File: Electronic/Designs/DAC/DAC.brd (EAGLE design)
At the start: 50 x 50 mm, 36 parts

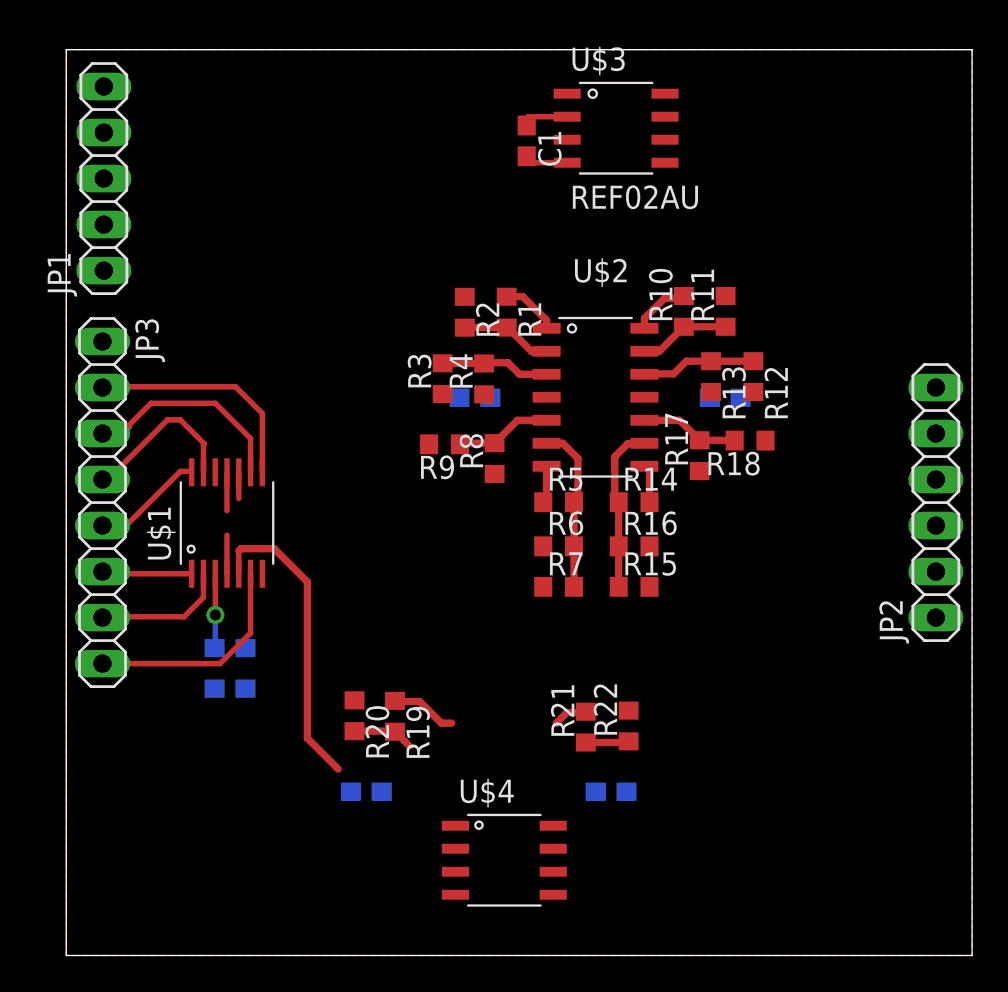
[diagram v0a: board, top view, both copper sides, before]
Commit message: adjusted adc pwr pins on board
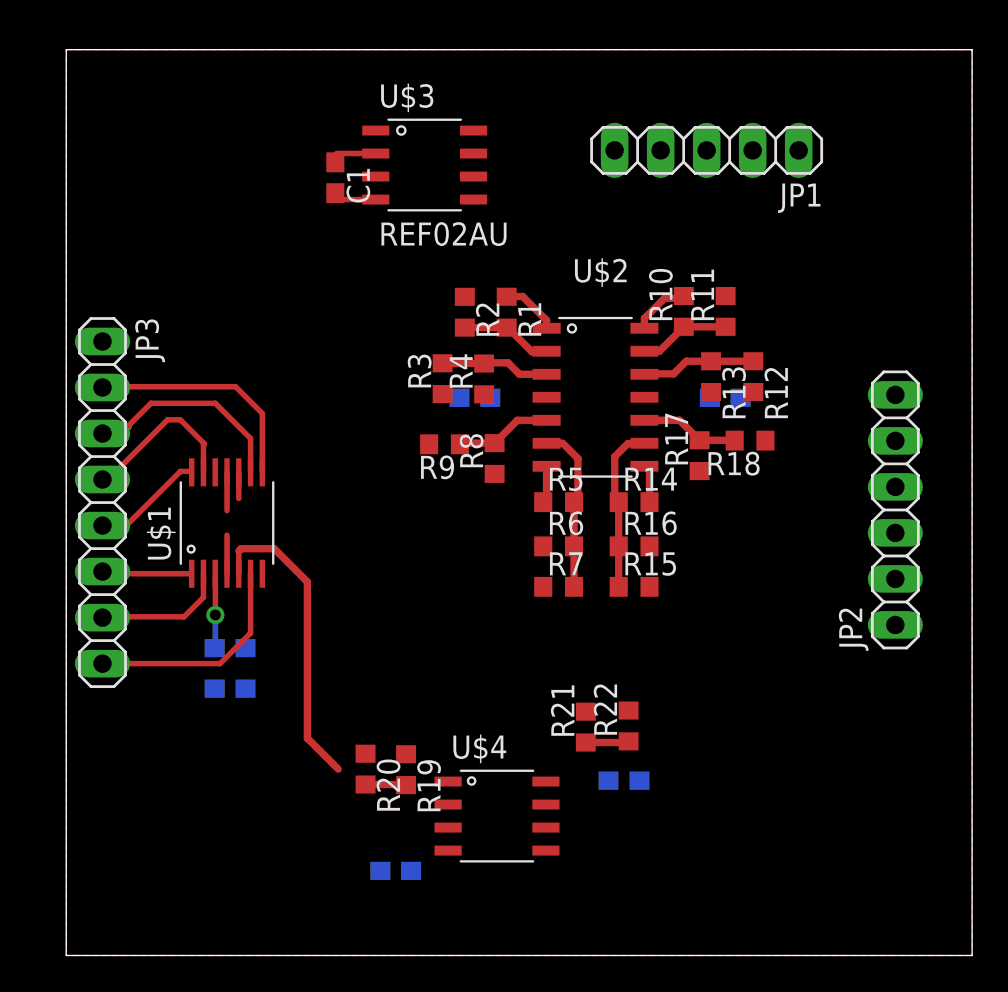
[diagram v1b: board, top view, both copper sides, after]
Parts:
- moved JP1 33.3 mm to (35.3, 44.4), turned to 180 degrees
- moved C7 14.2 mm to (30.8, 9.65), turned to 180 degrees
- moved C6 12.7 mm to (18.2, 4.67), turned to 0 degrees
- moved C1 10.8 mm to (14.9, 42.9)
- moved U$3 10.8 mm to (19.8, 43.0)
- moved R19 3.01 mm to (18.8, 10.3)
- moved R20 3.01 mm to (16.5, 10.3)
- moved U$4 2.47 mm to (23.8, 8.33)
- moved JP2 2.27 mm to (45.8, 24.6)
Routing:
- net N$21: track 3.64 -> 0.00 mm
- net BIAS: track 1.89 -> 0.00 mm
- net N$19: track 3.38 -> 2.25 mm

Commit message: split power pins from 5v and 15v
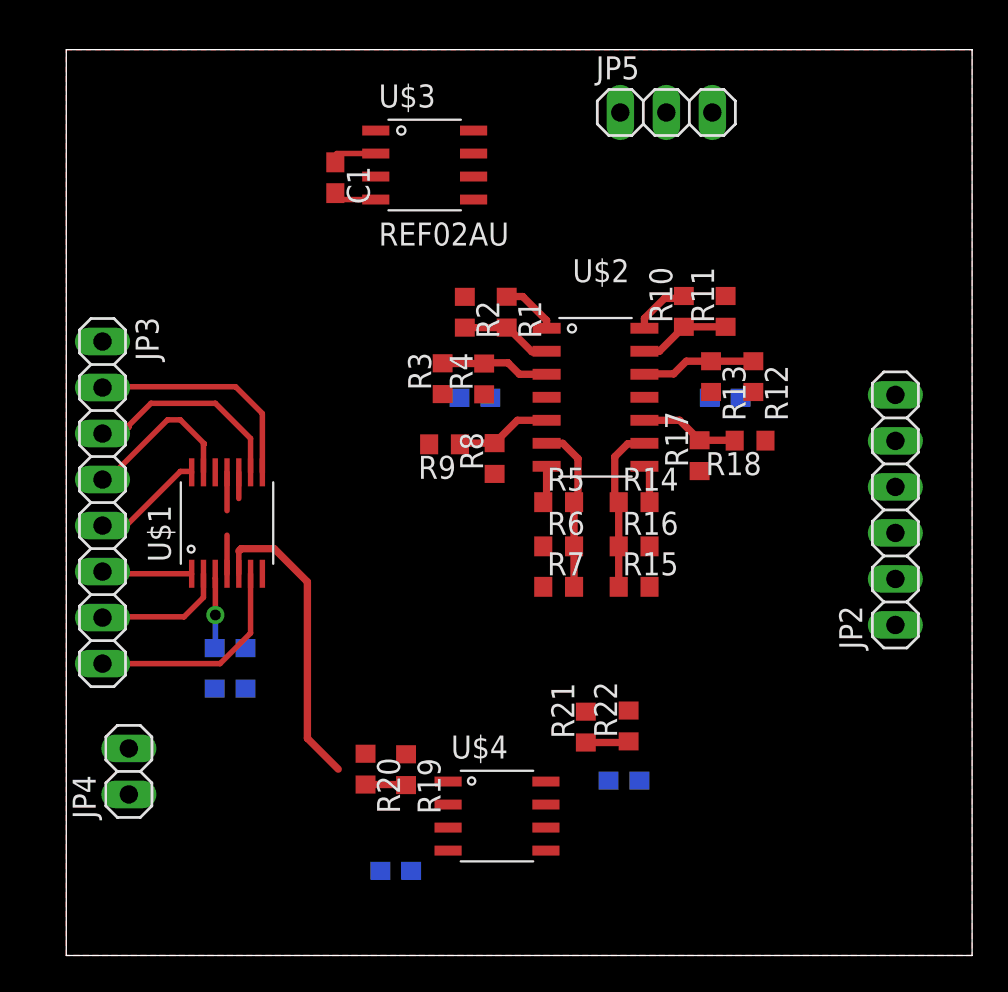
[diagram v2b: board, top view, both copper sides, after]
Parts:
- removed JP1: PWR, pinhead:1X05
- added JP4: (no value), pinhead:1X02
- added JP5: (no value), pinhead:1X03
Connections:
- net +15V: now also JP5.1; no longer JP1.4
- net +5V: now also JP4.2; no longer JP1.2
- net -15V: now also JP5.2; no longer JP1.5
- net GND: now also JP4.1, JP5.3; no longer JP1.1, JP1.3
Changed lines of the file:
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@@
 <elements>
 <element name="C1" library="resistor" package="C0603" value="0.1uf" x="14.8504" y="42.9308" rot="R270"/>
-<element name="JP1" library="pinhead" package="1X05" value="PWR" x="35.348" y="44.44" rot="R180"/>
 <element name="R1" library="resistor" package="R0603" value="40k" x="24.3116" y="35.5092" rot="R270"/>
 <element name="R10" library="resistor" package="R0603" value="40k" x="34.0896" y="35.5524" rot="R90"/>
@@
 <element name="C7" library="resistor" package="C0603" value="1uf" x="30.7848" y="9.652" rot="MR180"/>
 <element name="U$4" library="OPAX22X" package="SOIC-8" value="OPA2227UA" x="23.7744" y="8.3312"/>
+<element name="JP4" library="pinhead" package="1X02" value="" x="3.4544" y="10.16" rot="R90"/>
+<element name="JP5" library="pinhead" package="1X03" value="" x="33.1216" y="46.5328"/>
 </elements>
 <signals>
 <signal name="+5V">
 <contactref element="C3" pad="1"/>
-<contactref element="JP1" pad="2"/>
 <contactref element="U$1" pad="P$3"/>
 <contactref element="C2" pad="1"/>
@@
 <wire x1="8.2296" y1="18.796" x2="8.2296" y2="17.0044" width="0.3048" layer="16"/>
 <wire x1="8.2296" y1="17.0044" x2="8.1924" y2="16.9672" width="0.3048" layer="16"/>
-<wire x1="8.2228" y1="21.0704" x2="37.888" y2="44.44" width="0" layer="19" extent="1-1"/>
+<contactref element="JP4" pad="2"/>
 <wire x1="8.2228" y1="20.8348" x2="8.2228" y2="21.0704" width="0" layer="19" extent="1-1"/>
 <wire x1="8.1924" y1="14.732" x2="8.1924" y2="16.9672" width="0" layer="19" extent="16-16"/>
+<wire x1="3.4544" y1="11.43" x2="8.1924" y2="14.732" width="0" layer="19" extent="16-16"/>
 </signal>
 <signal name="-15V">
-<contactref element="JP1" pad="5"/>
 <contactref element="C5" pad="1"/>
 <contactref element="C6" pad="1"/>
 <contactref element="U$4" pad="P$4"/>
 <contactref element="U$2" pad="P$11"/>
-<wire x1="31.9128" y1="30.812" x2="30.268" y2="44.44" width="0" layer="19" extent="1-1"/>
+<contactref element="JP5" pad="2"/>
+<wire x1="31.9128" y1="30.812" x2="33.1216" y2="46.5328" width="0" layer="19" extent="1-1"/>
 <wire x1="23.4052" y1="30.7848" x2="31.9128" y2="30.812" width="0" layer="19" extent="1-16"/>
 <wire x1="21.0744" y1="5.7912" x2="23.4052" y2="30.7848" width="0" layer="19" extent="1-16"/>
@@
 <wire x1="17.0828" y1="44.2672" x2="14.9304" y2="44.2672" width="0.3048" layer="1"/>
 <wire x1="14.9304" y1="44.2672" x2="14.8504" y2="43.7808" width="0.3048" layer="1"/>
-<contactref element="JP1" pad="4"/>
 <contactref element="C4" pad="1"/>
 <contactref element="C7" pad="1"/>
 <contactref element="U$4" pad="P$8"/>
 <contactref element="U$2" pad="P$4"/>
-<wire x1="35.5228" y1="30.7848" x2="32.808" y2="44.44" width="0" layer="19" extent="16-16"/>
-<wire x1="26.5128" y1="30.812" x2="35.5228" y2="30.7848" width="0" layer="19" extent="1-16"/>
-<wire x1="17.0828" y1="44.2672" x2="32.808" y2="44.44" width="0" layer="19" extent="1-1"/>
+<contactref element="JP5" pad="1"/>
+<wire x1="17.0828" y1="44.2672" x2="30.5816" y2="46.5328" width="0" layer="19" extent="1-1"/>
+<wire x1="26.5128" y1="30.812" x2="30.5816" y2="46.5328" width="0" layer="19" extent="1-1"/>
+<wire x1="35.5228" y1="30.7848" x2="26.5128" y2="30.812" width="0" layer="19" extent="1-16"/>
 <wire x1="26.4744" y1="9.6012" x2="26.5128" y2="30.812" width="0" layer="19" extent="1-1"/>
 <wire x1="29.9348" y1="9.652" x2="26.4744" y2="9.6012" width="0" layer="19" extent="1-16"/>
@@
 <contactref element="C6" pad="2"/>
 <contactref element="C7" pad="2"/>
-<contactref element="JP1" pad="1"/>
-<contactref element="JP1" pad="3"/>
 <polygon width="0.4064" layer="1">
 <vertex x="0" y="50"/>
@@
 <vertex x="0" y="0"/>
 </polygon>
+<contactref element="JP4" pad="1"/>
+<contactref element="JP5" pad="3"/>
 <wire x1="35.5892" y1="31.1032" x2="37.2228" y2="30.7848" width="0" layer="19" extent="1-16"/>
 <wire x1="21.7052" y1="30.7848" x2="23.0668" y2="30.9752" width="0" layer="19" extent="1-16"/>
 <wire x1="31.6348" y1="9.652" x2="31.0408" y2="13.5196" width="0" layer="19" extent="1-16"/>
-<wire x1="9.8924" y1="16.9672" x2="8.2228" y2="26.6704" width="0" layer="19" extent="1-16"/>
-<wire x1="9.8924" y1="14.732" x2="9.8924" y2="16.9672" width="0" layer="19" extent="16-16"/>
+<wire x1="9.8924" y1="14.732" x2="3.4544" y2="8.89" width="0" layer="19" extent="16-16"/>
+<wire x1="9.8924" y1="16.9672" x2="9.8924" y2="14.732" width="0" layer="19" extent="16-16"/>
 <wire x1="17.3364" y1="4.6736" x2="9.8924" y2="14.732" width="0" layer="19" extent="16-16"/>
 </signal>

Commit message: added to dac pcb
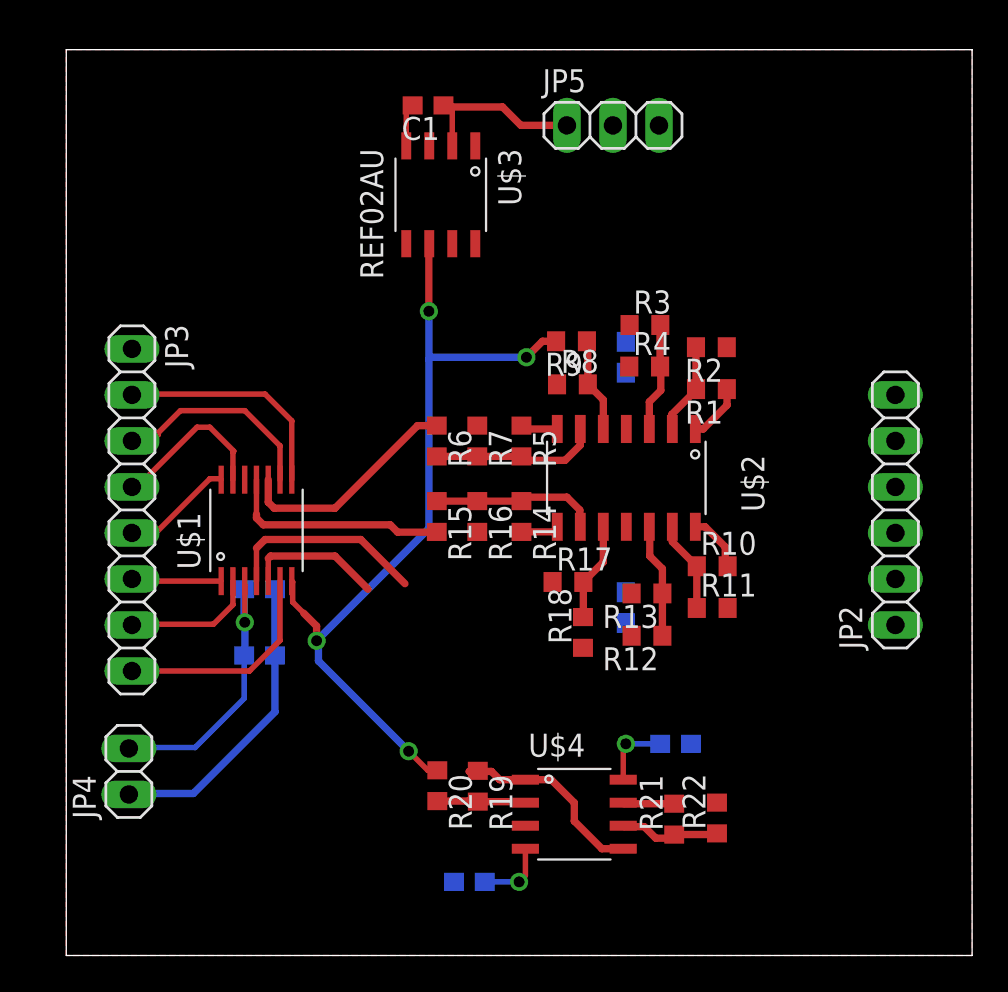
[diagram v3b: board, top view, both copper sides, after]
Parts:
- moved R11 16.4 mm to (35.7, 19.2), turned to 0 degrees
- moved R12 15.5 mm to (32.1, 17.6), turned to 180 degrees
- moved R10 14.2 mm to (35.7, 21.5), turned to 0 degrees
- moved R18 14.0 mm to (28.5, 17.8), turned to 90 degrees
- moved R2 13.7 mm to (35.6, 33.6), turned to 180 degrees
- moved C4 12.8 mm to (30.9, 19.2), turned to 270 degrees
- moved R13 12.5 mm to (32.1, 20.0), turned to 180 degrees
- moved R1 12.1 mm to (35.6, 31.3), turned to 180 degrees
- moved R15 11.6 mm to (20.5, 24.2), turned to 270 degrees
- moved R3 11.6 mm to (31.9, 34.8), turned to 0 degrees
- moved R17 10.1 mm to (27.7, 20.6), turned to 0 degrees
- moved R7 9.22 mm to (22.7, 28.4), turned to 270 degrees
- moved R9 9.03 mm to (27.9, 33.9)
- moved R6 8.89 mm to (20.5, 28.4), turned to 270 degrees
- moved R4 8.89 mm to (31.9, 32.5), turned to 0 degrees
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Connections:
- net X: now also U$1.P$10; no longer U$1.P$11
- net Y: now also U$1.P$11; no longer U$1.P$10
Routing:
- net VREF: track 0.00 -> 46.0 mm, vias 0 -> 4
- net GND: track 2.64 -> 19.4 mm
- net +5V: track 3.89 -> 15.6 mm
- net N$21: track 0.00 -> 11.3 mm
- net Y: track 1.45 -> 12.4 mm
- net +15V: track 2.65 -> 13.3 mm, vias 0 -> 1
- net X: track 2.12 -> 12.6 mm
- net B: track 16.9 -> 7.58 mm
- net Z: track 2.13 -> 11.2 mm
- net -15V: track 0.00 -> 3.87 mm, vias 0 -> 1
- net N$22: track 2.65 -> 5.55 mm
- net BIAS: track 0.00 -> 2.84 mm
- net N$19: track 2.25 -> 4.89 mm
